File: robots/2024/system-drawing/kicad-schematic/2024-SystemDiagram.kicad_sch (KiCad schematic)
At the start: 207 parts

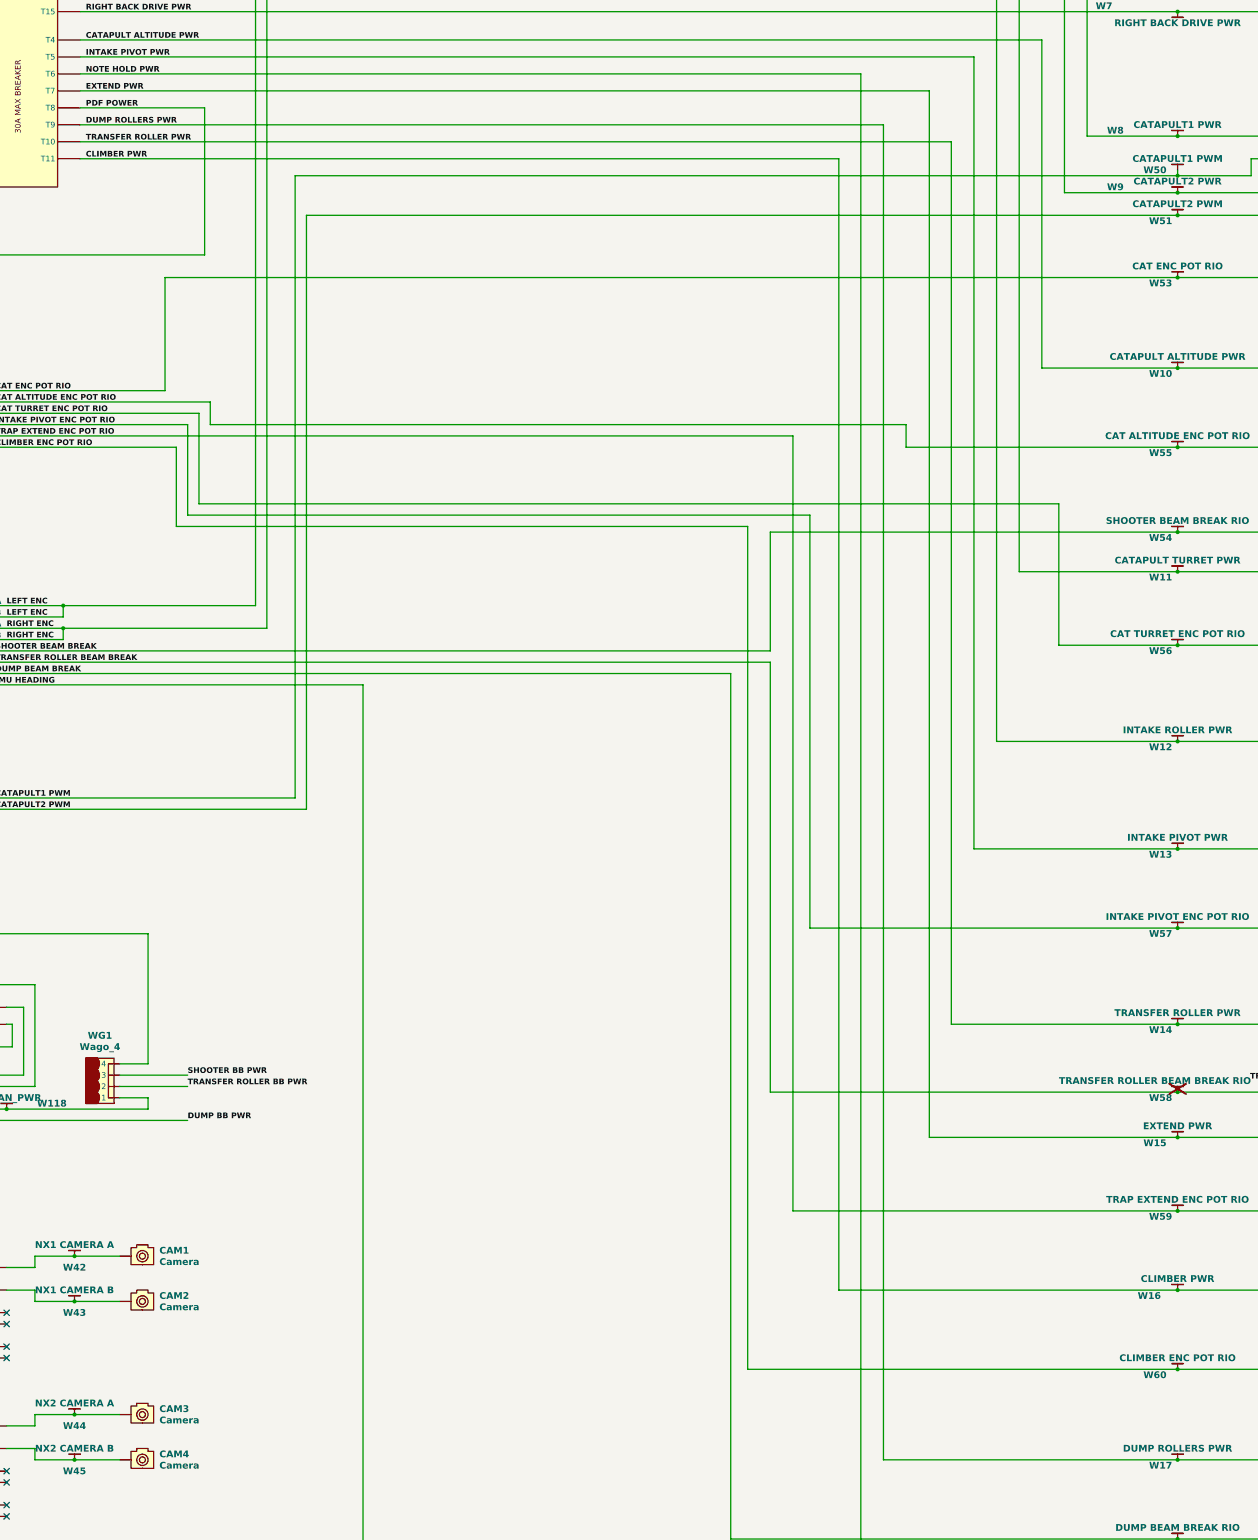
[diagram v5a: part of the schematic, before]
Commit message: Swapped Dump and Extend inputs to PDB on system dwg
Signed-off-by: Scott Berman <sgberman1@gmail.com>
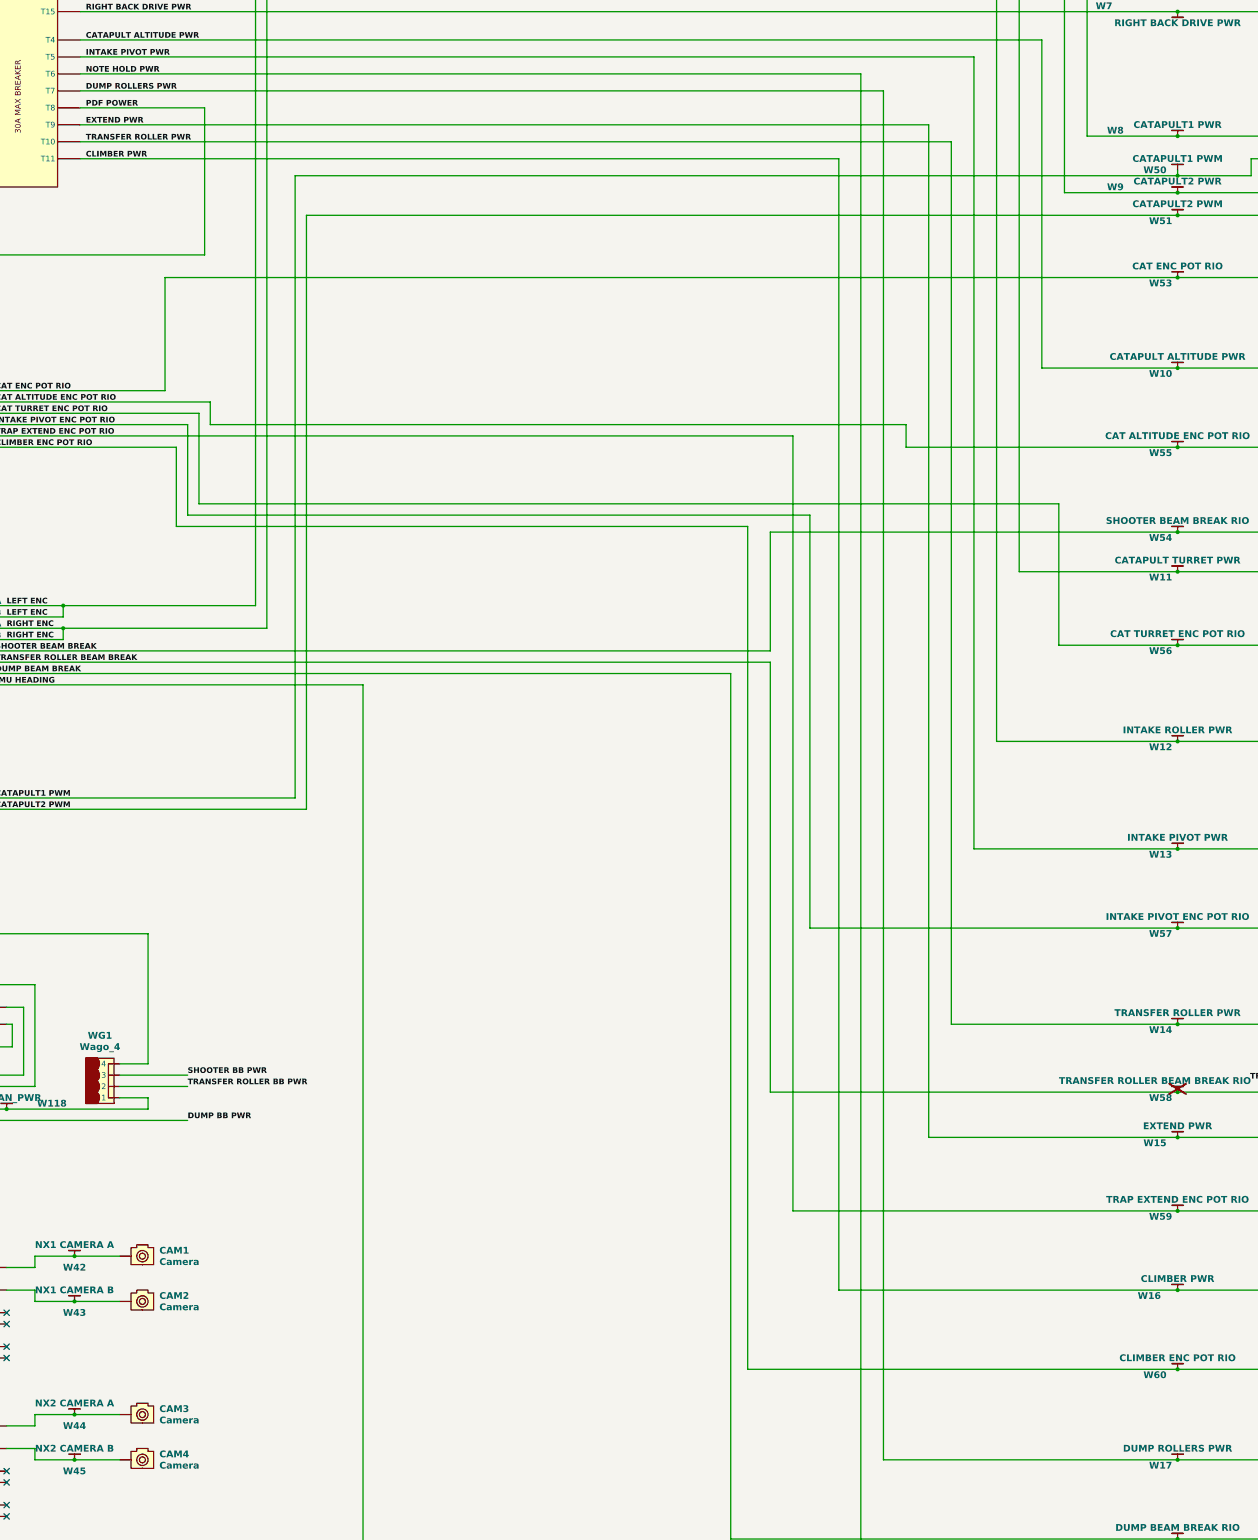
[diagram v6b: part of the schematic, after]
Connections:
- net DUMP ROLLERS PWR: now also PD1.T7; no longer PD1.T9
- net EXTEND PWR: now also PD1.T9; no longer PD1.T7
- net at POE1. (RJ45S): now also RDO1. (POWER); no longer VRM1. (5V/2A)
- net at RDO1. (POWER): now also ETH1. (POWER); no longer VRM1. (5V/2A)
- net at ETH1. (POWER): now also NX1. (Power), W87.; no longer RDO1. (POWER)
- new net: VRM1. (5V/2A), W118., WG1. (4)
- new net: POE1. (RJ45S), VRM1. (5V/2A)
- new net: RDO1. (POWER), VRM1. (5V/2A)
- new net: CAN1. (USB), W67., WG1. (4)
- new net: ETH1. (POWER), NX2. (Power), W88.
- new net: MOT10. (PWR), MOT12. (PWR), W111.
- new net: VRM2. (5V/2A), W85., WG101. (3)
- new net: ETH1. (POWER), VRM2. (5V/2A), W84.
- new net: ETH1. (POWER), NX3. (Power), W89.
- new net: PD2. (IN), WG101. (3)
- new net: MOT1. (PWR), MOT2. (PWR), W105.
- new net: MOT3. (PWR), MOT4. (PWR), W107.
- new net: IMU1. (RIO_PWM2), NX3. (Power), W47.
- now unconnected: VRM2. (5V/2A), VRM2. (5V/2A)
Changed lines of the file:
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@@
   (junction (at 487.68 452.12) (diameter 0) (color 0 0 0 0)
   )
-  (junction (at 487.68 351.79) (diameter 0) (color 255 0 0 1)
-  )
   (junction (at 487.68 179.07) (diameter 0) (color 0 0 0 0)
   )
   (junction (at 487.68 72.39) (diameter 0) (color 255 0 0 1)
+  )
+  (junction (at 487.68 351.79) (diameter 0) (color 0 0 0 0)
   )
   (junction (at 510.54 144.78) (diameter 0) (color 0 0 0 0)
@@
     (stroke (width 0.508) (type default) (color 255 0 0 1))
   )
-  (wire (pts (xy 431.9411 116.84) (xy 241.3 116.84))
-    (stroke (width 0.508) (type default) (color 255 0 0 1))
-  )
   (wire (pts (xy 580.39 407.67) (xy 575.31 407.67))
     (stroke (width 0) (type default))
@@
     (stroke (width 0.508) (type default) (color 255 0 0 1))
   )
+  (wire (pts (xy 431.8 124.46) (xy 431.8 351.79))
+    (stroke (width 0.508) (type default) (color 255 0 0 1))
+  )
+  (wire (pts (xy 241.3 116.84) (xy 421.64 116.84))
+    (stroke (width 0.508) (type default) (color 255 0 0 1))
+  )
   (wire (pts (xy 590.55 474.98) (xy 596.9 474.98))
     (stroke (width 0.254) (type default) (color 255 153 0 1))
@@
     (stroke (width 0) (type default))
   )
-  (wire (pts (xy 421.64 124.46) (xy 241.3 124.46))
-    (stroke (width 0.508) (type default) (color 255 0 0 1))
-  )
   (wire (pts (xy 124.46 452.12) (xy 171.45 452.12))
     (stroke (width 0.508) (type default) (color 255 0 0 1))
@@
     (stroke (width 0.508) (type default) (color 255 0 0 1))
   )
-  (wire (pts (xy 431.9411 351.79) (xy 431.9411 116.84))
-    (stroke (width 0.508) (type default) (color 255 0 0 1))
-  )
   (wire (pts (xy 416.56 521.97) (xy 171.45 521.97))
     (stroke (width 0.508) (type default) (color 255 0 0 1))
@@
   (wire (pts (xy 220.98 242.57) (xy 396.24 242.57))
     (stroke (width 0.254) (type default) (color 194 0 194 1))
-  )
-  (wire (pts (xy 487.68 351.79) (xy 431.9411 351.79))
-    (stroke (width 0.508) (type default) (color 255 0 0 1))
   )
   (wire (pts (xy 289.56 275.59) (xy 220.98 275.59))
@@
     (stroke (width 0.254) (type default) (color 255 153 0 1))
   )
-  (wire (pts (xy 421.64 424.18) (xy 421.64 124.46))
+  (wire (pts (xy 421.64 116.84) (xy 421.64 424.18))
     (stroke (width 0.508) (type default) (color 255 0 0 1))
   )
@@
     (stroke (width 0) (type default))
   )
+  (wire (pts (xy 241.3 124.46) (xy 431.8 124.46))
+    (stroke (width 0.508) (type default) (color 255 0 0 1))
+  )
   (wire (pts (xy 598.17 41.91) (xy 598.17 40.64))
     (stroke (width 0) (type default))
@@
     (stroke (width 0) (type default))
   )
+  (wire (pts (xy 431.8 351.79) (xy 487.68 351.79))
+    (stroke (width 0.508) (type default) (color 255 0 0 1))
+  )
   (wire (pts (xy 270.51 191.77) (xy 270.51 186.69))
     (stroke (width 0.254) (type default) (color 194 0 194 1))
@@
     (effects (font (face "FreeSans") (size 1.27 1.27) bold) (justify right bottom))
   )
-  (label "DUMP ROLLERS PWR" (at 242.57 124.46 0) (fields_autoplaced)
-    (effects (font (face "FreeSans") (size 1.27 1.27) bold) (justify left bottom))
-  )
   (label "CAN_PD" (at 601.98 388.62 180) (fields_autoplaced)
     (effects (font (face "FreeSans") (size 1.27 1.27) bold) (justify right bottom))
@@
   )
   (label "NOTE HOLD PWR" (at 242.57 113.03 0) (fields_autoplaced)
+    (effects (font (face "FreeSans") (size 1.27 1.27) bold) (justify left bottom))
+  )
+  (label "EXTEND PWR" (at 242.57 124.46 0) (fields_autoplaced)
     (effects (font (face "FreeSans") (size 1.27 1.27) bold) (justify left bottom))
   )
@@
     (effects (font (face "FreeSans") (size 1.27 1.27) bold) (justify right bottom))
   )
-  (label "EXTEND PWR" (at 242.57 116.84 0) (fields_autoplaced)
-    (effects (font (face "FreeSans") (size 1.27 1.27) bold) (justify left bottom))
-  )
   (label "INTAKE PIVOT ENC POT RIO" (at 222.25 191.77 0) (fields_autoplaced)
     (effects (font (face "FreeSans") (size 1.27 1.27) bold) (justify left bottom))
@@
     (effects (font (face "FreeSans") (size 1.27 1.27) bold) (justify left bottom))
   )
+  (label "DUMP ROLLERS PWR" (at 242.57 116.84 0) (fields_autoplaced)
+    (effects (font (face "FreeSans") (size 1.27 1.27) bold) (justify left bottom))
+  )
